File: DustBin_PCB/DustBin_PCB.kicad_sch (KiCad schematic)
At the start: 13 parts, among them U1 XIAO-SAMD21-DIP, U2 DFR0299

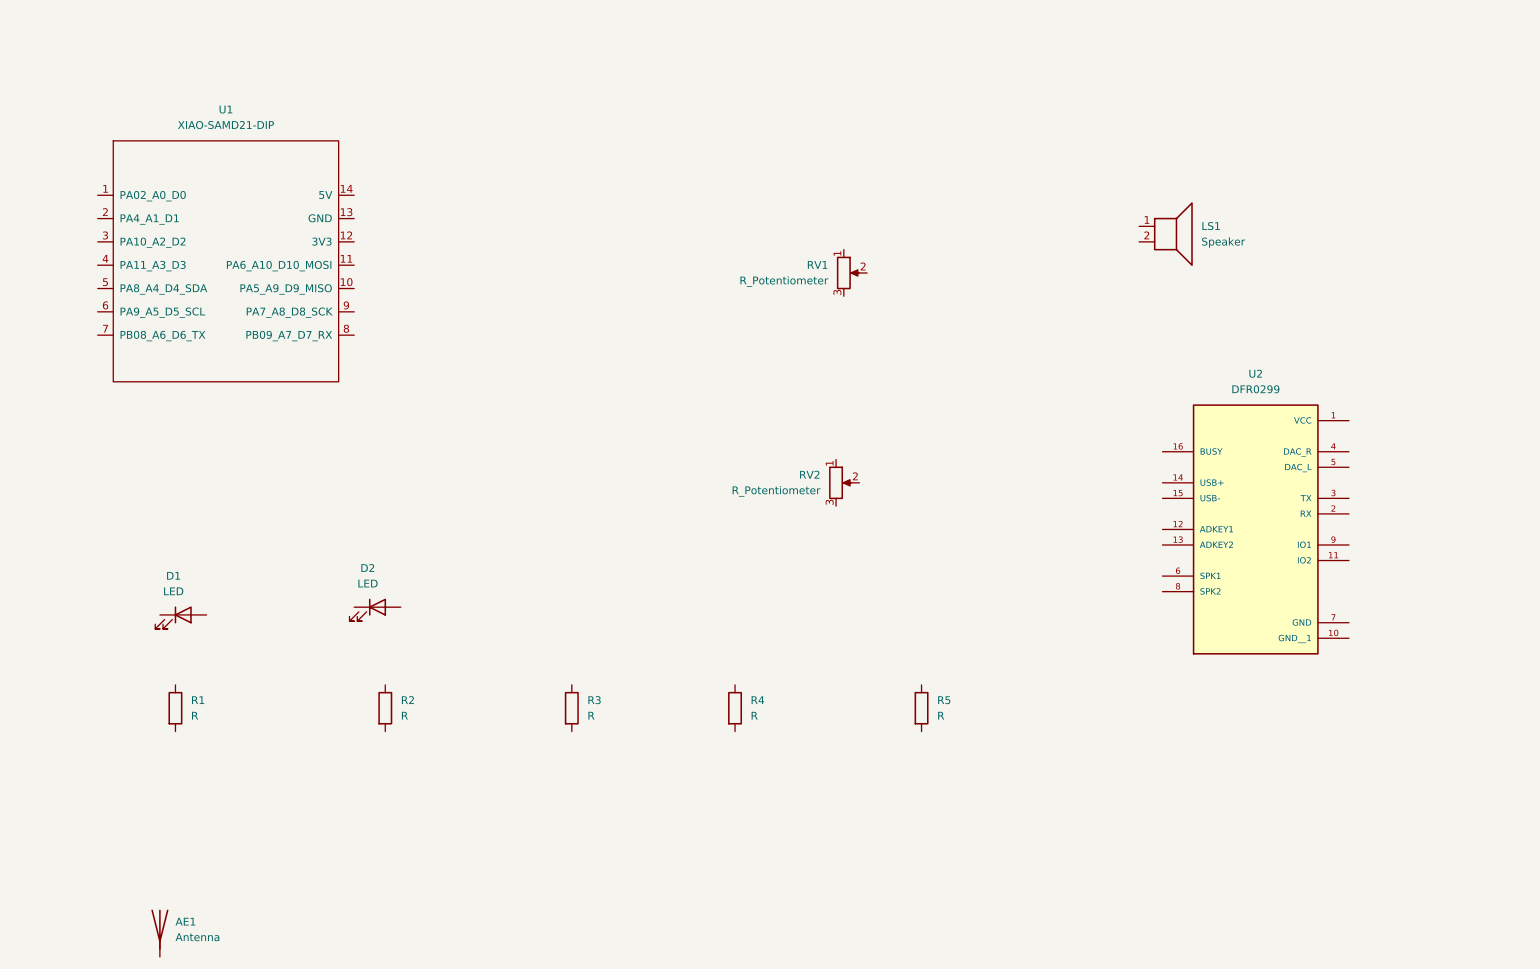
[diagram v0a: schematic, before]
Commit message: Including more kicad files and improving the potentiometer adjustment code
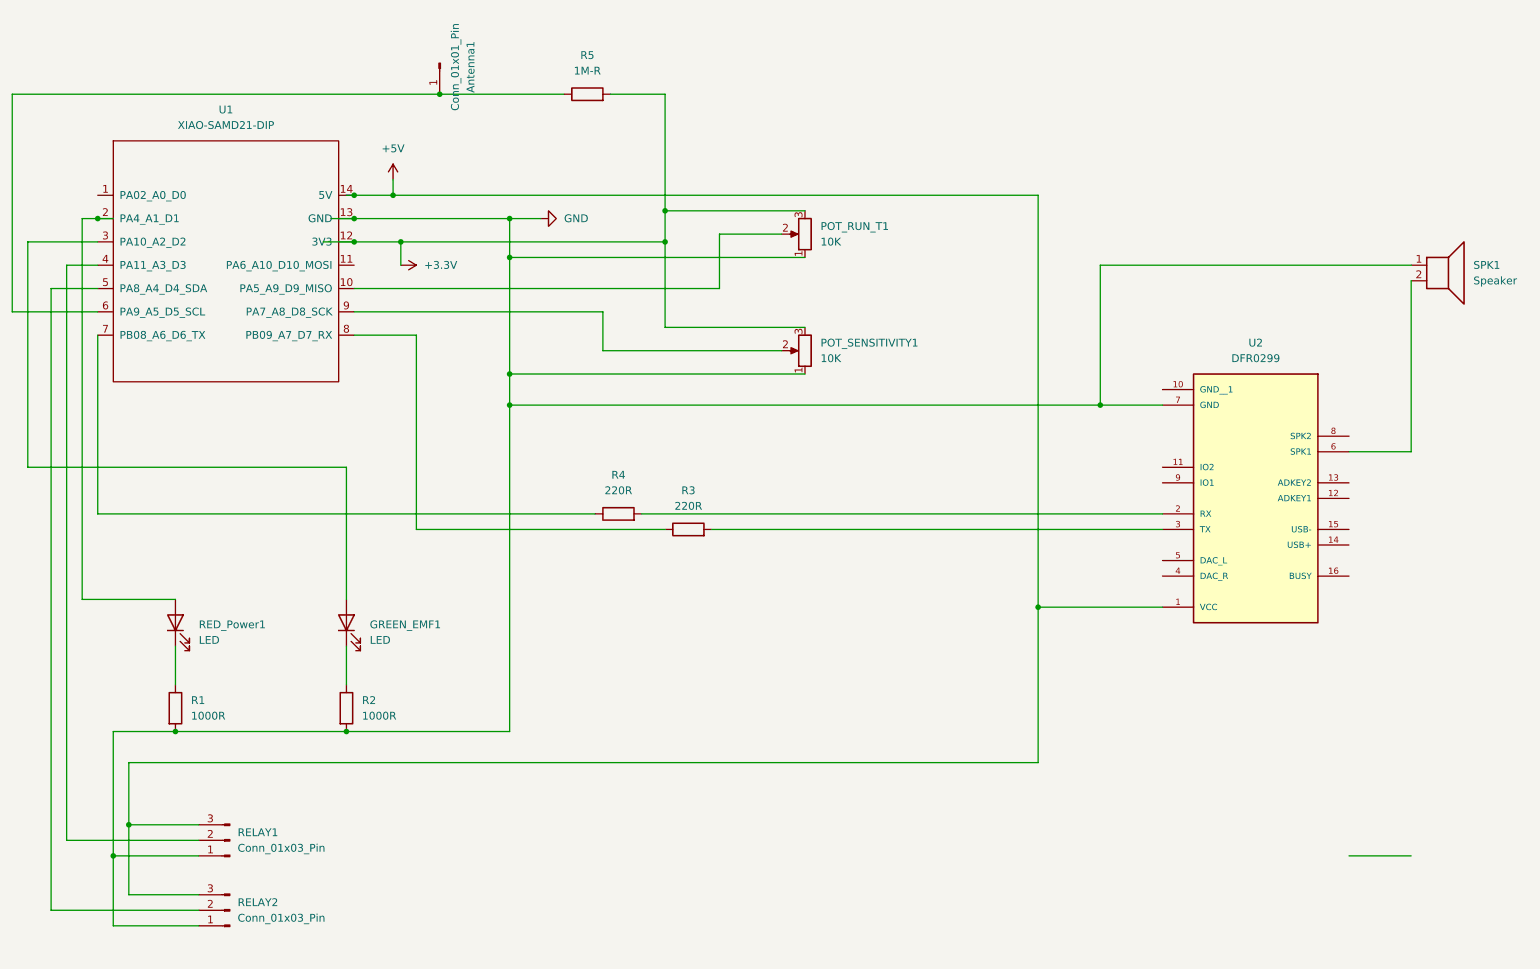
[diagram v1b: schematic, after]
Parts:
- removed AE1: Antenna, symbol Device:Antenna
- removed RV2: R_Potentiometer, symbol Device:R_Potentiometer
- added Antenna1: Conn_01x01_Pin, Connector_PinHeader_2.54mm:PinHeader_1x01_P2.54mm_Vertical, symbol Connector:Conn_01x01_Pin
- added POT_SENSITIVITY1: 10K, Potentiometer_THT:JG-3Pin-Pot-11mmOuterPins, symbol Device:R_Potentiometer
- added RELAY1, RELAY2: Conn_01x03_Pin, Connector_PinHeader_2.54mm:PinHeader_1x03_P2.54mm_Vertical, symbol Connector:Conn_01x03_Pin
- GREEN_EMF1: renamed from D2; footprint (none) -> LED_THT:LED_D5.0mm
- POT_RUN_T1: renamed from RV1; value R_Potentiometer -> 10K; footprint (none) -> Potentiometer_THT:JG-3Pin-Pot-11mmOuterPins
- R1, R2: value R -> 1000R; footprint (none) -> Resistor_THT:R_Axial_DIN0207_L6.3mm_D2.5mm_P10.16mm_Horizontal
- R3, R4: value R -> 220R; footprint (none) -> Resistor_THT:R_Axial_DIN0207_L6.3mm_D2.5mm_P10.16mm_Horizontal
- R5: value R -> 1M-R; footprint (none) -> Resistor_THT:R_Axial_DIN0207_L6.3mm_D2.5mm_P10.16mm_Horizontal
- RED_Power1: renamed from D1; footprint (none) -> LED_THT:LED_D5.0mm
- SPK1: renamed from LS1; footprint (none) -> Connector_PinHeader_2.54mm:PinHeader_1x02_P2.54mm_Vertical
- U1: footprint (none) -> Seeed Studio XIAO Series Library:XIAO-SAMD21-DIP
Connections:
- net GND: now reaches POT_RUN_T1.1
- net GND: now also R1.2, R2.2, SPK1.1, U1.13 (GND), U2.7 (GND), POT_SENSITIVITY1.1, RELAY1.1 (Pin_1), RELAY2.1 (Pin_1)
- net at POT_RUN_T1.2: now also U1.10 (PA5_A9_D9_MISO)
- net +3.3V: now reaches POT_RUN_T1.3
- net +3.3V: now also R5.2, U1.12 (3V3), POT_SENSITIVITY1.3
- net at SPK1.2: now also U2.6 (SPK1)
- net at R2.1: now also GREEN_EMF1.1 (K)
- net at R5.1: now also U1.6 (PA9_A5_D5_SCL), Antenna1.1 (Pin_1)
- net +5V: now reaches U2.1 (VCC)
- net +5V: now also U1.14 (5V), RELAY1.3 (Pin_3), RELAY2.3 (Pin_3)
- net at U2.2 (RX): now also R4.2
- net at U2.3 (TX): now also R3.2
- net at U1.2 (PA4_A1_D1): now also RED_Power1.2 (A)
- net at U1.3 (PA10_A2_D2): now also GREEN_EMF1.2 (A)
- net at U1.4 (PA11_A3_D3): now also RELAY1.2 (Pin_2)
- net at U1.5 (PA8_A4_D4_SDA): now also RELAY2.2 (Pin_2)
- net at U1.7 (PB08_A6_D6_TX): now also R4.1
- net at U1.8 (PB09_A7_D7_RX): now also R3.1
- net at U1.9 (PA7_A8_D8_SCK): now also POT_SENSITIVITY1.2
- net at RED_Power1.1 (K): now also R1.1
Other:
- moved on the sheet: GREEN_EMF1, POT_RUN_T1, RED_Power1, SPK1, U2
